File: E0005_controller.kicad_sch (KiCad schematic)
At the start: 0 parts

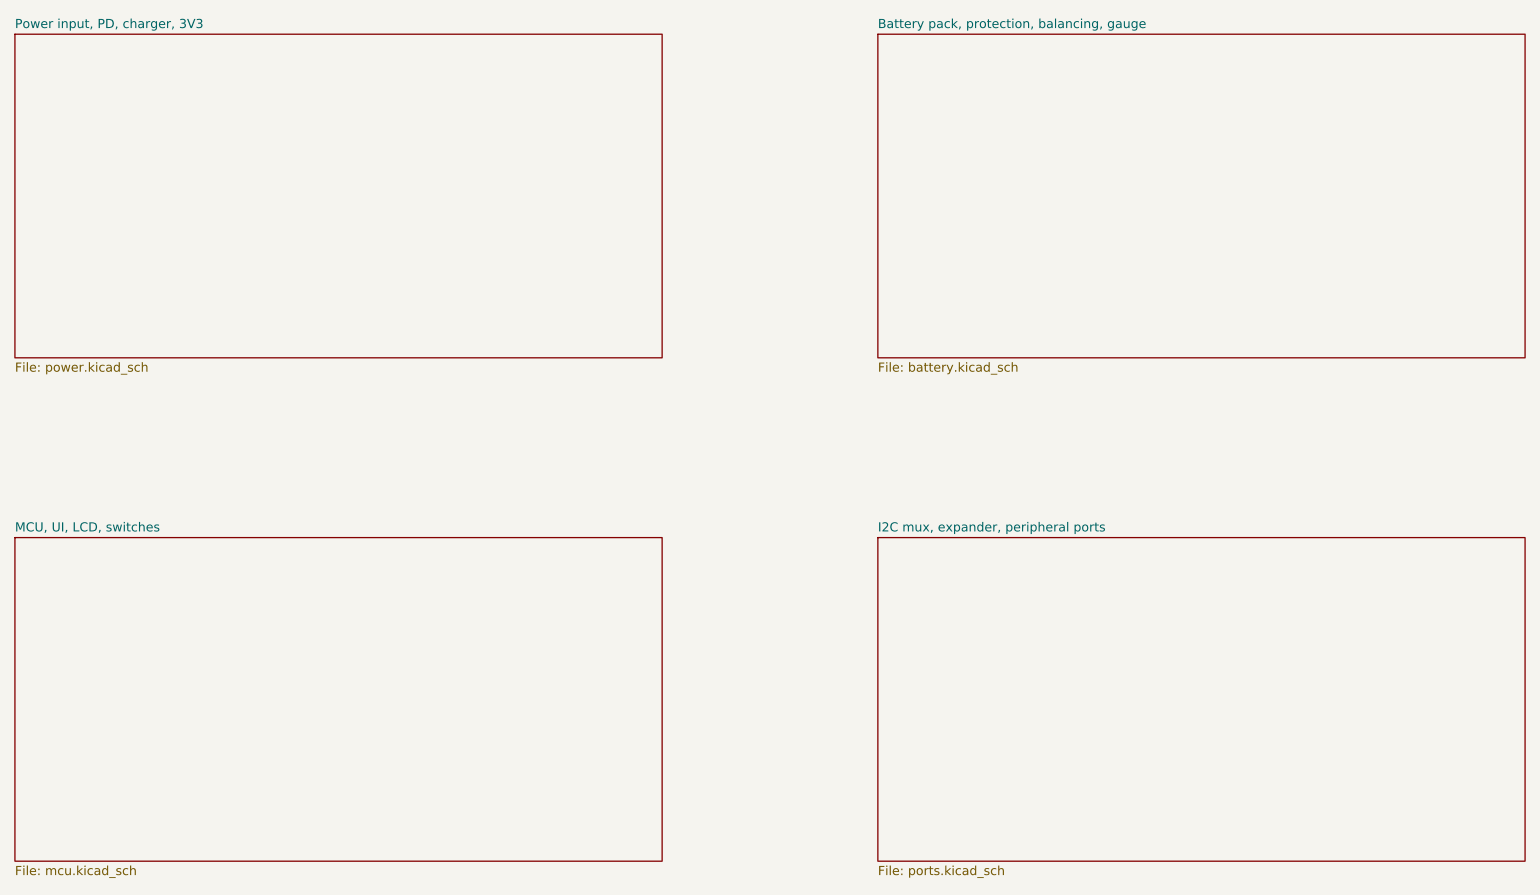
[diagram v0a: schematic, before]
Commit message: E0005 schematic: all four sheets captured for SPEC v1.0, ERC 0
- power: USB-C CC Rd + ADC sense, U_IN TPS259470A with 3-level ILM legs, BQ25887 charger,
  TPS56637 2S->5 V buck with soft power latch, V5 sense, TPS629210 3V3 from V5
- battery: BQ29209/OV2/MID divider removed (owner Q2)
- mcu: SPEC 7 pin map (GPIO4/6/7 ADC, GPIO36 PWR_HOLD, GPIO48 EXP_INT_N), 9 V ESD on PB_RAW
- ports: 5 V OVLO/UVLO dividers, SMF5.0A, 10 uF at each eFuse input
- lib: TPS56637 symbol + TI RPA0010A footprint; E0003 references kept for unchanged parts

Co-Authored-By: Claude Opus 5.5 <noreply@anthropic.com>
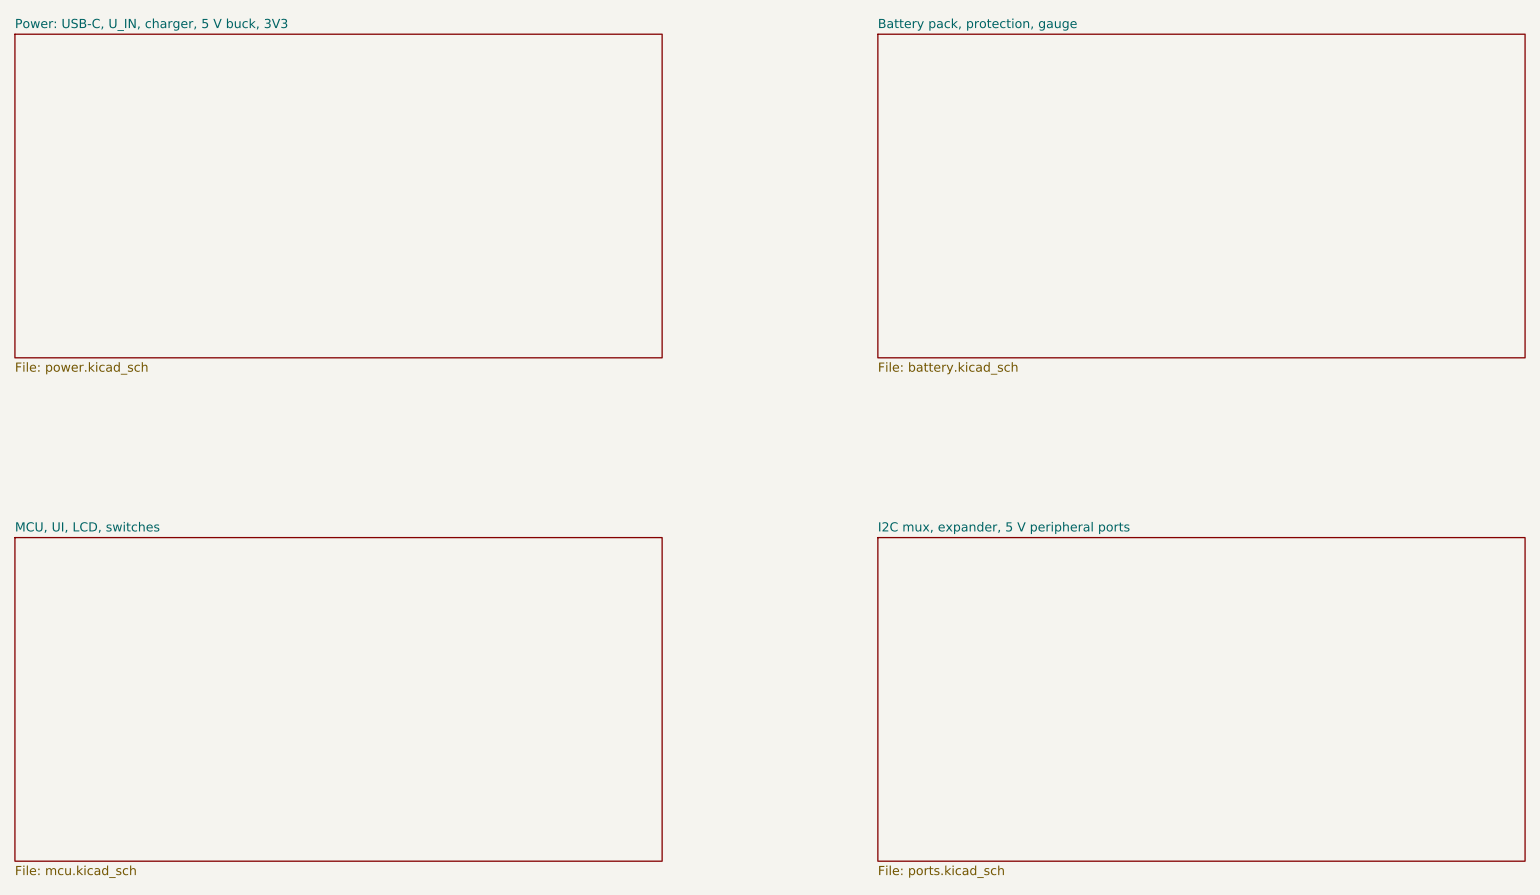
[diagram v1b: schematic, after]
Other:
- removed sheet Battery pack, protection, balancing, gauge
- removed sheet I2C mux, expander, peripheral ports
- removed sheet Power input, PD, charger, 3V3
- added sheet Battery pack, protection, gauge (battery.kicad_sch)
- added sheet I2C mux, expander, 5 V peripheral ports (ports.kicad_sch)
- added sheet Power: USB-C, U_IN, charger, 5 V buck, 3V3 (power.kicad_sch)
- title: E0003 ESP32 control box mainboard -> E0005 ESP32-S3 5 V controller
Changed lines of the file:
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@@
 	(paper "A4")
 	(title_block
-		(title "E0003 ESP32 control box mainboard")
-		(date "2026-10-11")
+		(title "E0005 ESP32-S3 5 V controller")
+		(date "2026-10-27")
 		(rev "A")
 		(company "")
-		(comment 1 "2S Molicel P50B, BQ25798 + STUSB4500, MAX17205 stack-only, 5 x TPS259470A ports")
-		(comment 2 "Spec docs/SPEC.md v1.2; generated by build/scripts/gen_sch.py")
+		(comment 1 "5 V USB-C (no PD), U_IN eFuse, BQ25887 2S charger, TPS56637 2S -> 5 V buck, MAX17205, 5 x 5 V ports")
+		(comment 2 "Spec docs/SPEC.md v1.0; generated by build/scripts/gen_sch.py")
 	)
 	(sheet
@@
 			(color 0 0 0 0)
 		)
-		(property "Sheetname" "Power input, PD, charger, 3V3"
+		(property "Sheetname" "Power: USB-C, U_IN, charger, 5 V buck, 3V3"
 			(at 20 29.3 0)
 			(effects
@@
 		(instances
 			(project "E0005_controller"
-				(path "/847558bb-a841-5667-996c-e9a177700ba5"
+				(path "/941c9a94-d85a-5574-b1cc-3e129393c8ae"
 					(page "2")
 				)
@@
 			(color 0 0 0 0)
 		)
-		(property "Sheetname" "Battery pack, protection, balancing, gauge"
+		(property "Sheetname" "Battery pack, protection, gauge"
 			(at 140 29.3 0)
 			(effects
@@
 		(instances
 			(project "E0005_controller"
-				(path "/847558bb-a841-5667-996c-e9a177700ba5"
+				(path "/941c9a94-d85a-5574-b1cc-3e129393c8ae"
 					(page "3")
 				)
@@
 		(instances
 			(project "E0005_controller"
-				(path "/847558bb-a841-5667-996c-e9a177700ba5"
+				(path "/941c9a94-d85a-5574-b1cc-3e129393c8ae"
 					(page "4")
 				)
@@
 			(color 0 0 0 0)
 		)
-		(property "Sheetname" "I2C mux, expander, peripheral ports"
+		(property "Sheetname" "I2C mux, expander, 5 V peripheral ports"
 			(at 140 99.3 0)
 			(effects
@@
 		(instances
 			(project "E0005_controller"
-				(path "/847558bb-a841-5667-996c-e9a177700ba5"
+				(path "/941c9a94-d85a-5574-b1cc-3e129393c8ae"
 					(page "5")
 				)
